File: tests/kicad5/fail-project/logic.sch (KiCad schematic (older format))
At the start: 4 parts

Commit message: Imported kicad5/fail-project with KiCad 5.1.5
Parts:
- C2: symbol passive:C -> fail-project-rescue:C-passive
- C3, C4: symbol passive:CP -> fail-project-rescue:CP-passive
- R1: symbol passive:R -> fail-project-rescue:R-passive
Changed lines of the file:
@@
 EESchema Schematic File Version 4
-LIBS:good-project-cache
-EELAYER 29 0
+EELAYER 30 0
 EELAYER END
 $Descr A4 11693 8268
@@
 $EndDescr
 $Comp
-L passive:R R1
+L fail-project-rescue:R-passive R1
 U 1 1 5CA75C86
 P 5500 2790
@@
 $EndComp
 $Comp
-L passive:C C2
+L fail-project-rescue:C-passive C2
 U 1 1 5CA76352
 P 5700 2860
@@
 VCC
 $Comp
-L passive:CP C3
+L fail-project-rescue:CP-passive C3
 U 1 1 5CA7214E
 P 6110 2580
@@
 $EndComp
 $Comp
-L passive:CP C4
+L fail-project-rescue:CP-passive C4
 U 1 1 5CA735B9
 P 6320 2580

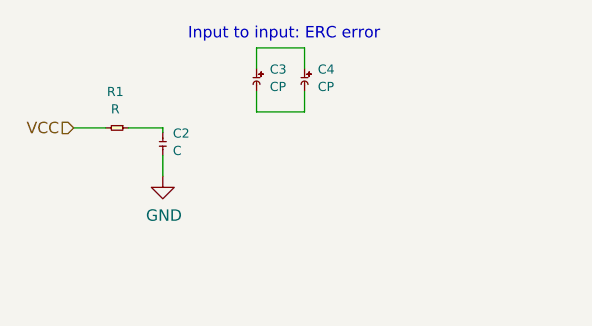
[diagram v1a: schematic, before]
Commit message: Fixed fail-project to really have an ERC error (not just warning) when using KiCad 5.
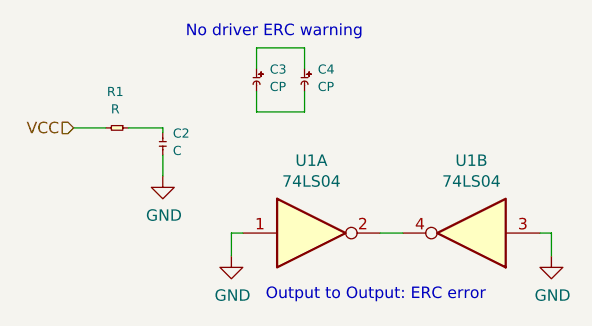
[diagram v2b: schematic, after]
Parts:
- added U1: 74LS04, symbol 74xx:74LS04
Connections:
- net GND: now also U1.1, U1.3
- new net: U1.2, U1.4
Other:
- note added: "No driver ERC warning"
- note added: "Output to Output: ERC error"
- note removed: "Input to input: ERC error"
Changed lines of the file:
@@
 Wire Wire Line
 	6110 2720 6110 2630
-Text Notes 5810 2410 0    50   ~ 0
-Input to input: ERC error
+Text Notes 6150 3550 0    50   ~ 0
+Output to Output: ERC error
+$Comp
+L 74xx:74LS04 U1
+U 1 1 5EAD683A
+P 6350 3250
+F 0 "U1" H 6350 3567 50  0000 C CNN
+F 1 "74LS04" H 6350 3476 50  0000 C CNN
+F 2 "" H 6350 3250 50  0001 C CNN
+F 3 "http://www.ti.com/lit/gpn/sn74LS04" H 6350 3250 50  0001 C CNN
+	1    6350 3250
+	1    0    0    -1
+$EndComp
+$Comp
+L 74xx:74LS04 U1
+U 2 1 5EAD766B
+P 7050 3250
+F 0 "U1" H 7050 2933 50  0000 C CNN
+F 1 "74LS04" H 7050 3024 50  0000 C CNN
+F 2 "" H 7050 3250 50  0001 C CNN
+F 3 "http://www.ti.com/lit/gpn/sn74LS04" H 7050 3250 50  0001 C CNN
+	2    7050 3250
+	-1   0    0    1
+$EndComp
+Wire Wire Line
+	6650 3250 6750 3250
+Wire Wire Line
+	6050 3250 6000 3250
+Wire Wire Line
+	6000 3250 6000 3350
+Wire Wire Line
+	7350 3250 7400 3250
+Wire Wire Line
+	7400 3250 7400 3350
+$Comp
+L power:GND #PWR05
+U 1 1 5EAD892D
+P 7400 3350
+F 0 "#PWR05" H 7400 3100 50  0001 C CNN
+F 1 "GND" H 7405 3177 50  0000 C CNN
+F 2 "" H 7400 3350 50  0001 C CNN
+F 3 "" H 7400 3350 50  0001 C CNN
+	1    7400 3350
+	1    0    0    -1
+$EndComp
+$Comp
+L power:GND #PWR04
+U 1 1 5EAD967D
+P 6000 3350
+F 0 "#PWR04" H 6000 3100 50  0001 C CNN
+F 1 "GND" H 6005 3177 50  0000 C CNN
+F 2 "" H 6000 3350 50  0001 C CNN
+F 3 "" H 6000 3350 50  0001 C CNN
+	1    6000 3350
+	1    0    0    -1
+$EndComp
+Text Notes 5800 2400 0    50   ~ 0
+No driver ERC warning
 $EndSCHEMATC
